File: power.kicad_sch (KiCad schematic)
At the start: 4 parts, among them J1 USB_C_Receptacle_USB2.0_16P, U2 USBLC6-2SC6

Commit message: add power
Signed-off-by: HaoboGu <haobogu@outlook.com>
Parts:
- added C1, C2: 10uf, symbol Device:C
- added C3, C4: 10uf, symbol Device:C_Polarized_Small_US
- added J2: Battery, Connector_JST:JST_SH_SM02B-SRSS-TB_1x02-1MP_P1.00mm_Horizontal, symbol Connector_Generic_Shielded:Conn_01x02_Shielded
- added R3: 3K, symbol Device:R
- added R4: 0.4, symbol Device:R
- added R5: 10K, symbol Device:R
- added SW62: SW_SPDT, symbol Switch:SW_SPDT
- added U3: TP4056, TP4056:ESOP-8_L4.9-W3.9-P1.27-LS6.0-BL-EP, symbol TP4056:TP4056_C725790
- added U4: AMS1117-3.3, Package_TO_SOT_SMD:SOT-223-3_TabPin2, symbol Regulator_Linear:AMS1117-3.3
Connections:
- net +5V: now also C4.1, R4.1, U4.3 (VI)
- net GND: now also C1.2, C2.2, C3.2, C4.2, J2.2 (Pin_2), J2.SH (Shield), R3.1, U3.1 (TEMP), U3.3 (GND), U4.1 (GND)
- new net: J2.1 (Pin_1), SW62.2 (B)
- new net: R5.2, SW62.3 (C)
- new net: R3.2, U3.2 (PROG)
- new net +3.3V: C3.1, U4.2 (VO)
- new net CHARGE: U3.7 (CHRG#)
- new net Li+: C1.1, SW62.1 (A), U3.5 (BAT)
- new net Vin: C2.1, R4.2, U3.4 (VCC), U3.8 (CE)
- no-connect marks 2 -> 5
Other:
- note added: "5V -> 3.3V"
- note added: "Battery"
- note added: "ESD"
- note added: "I_bat = 400ma"
- note added: "USB"
- moved on the sheet: J1, R1, R2, U2

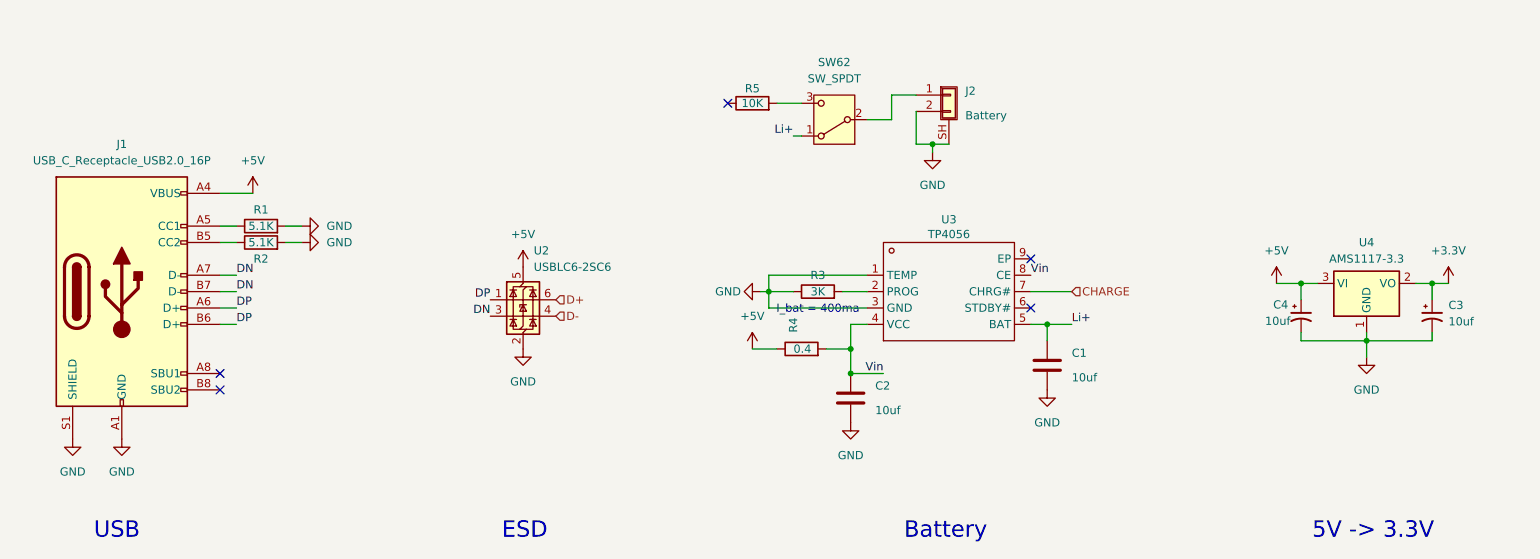
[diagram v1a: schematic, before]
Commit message: schema: rev0 done
Signed-off-by: HaoboGu <haobogu@outlook.com>
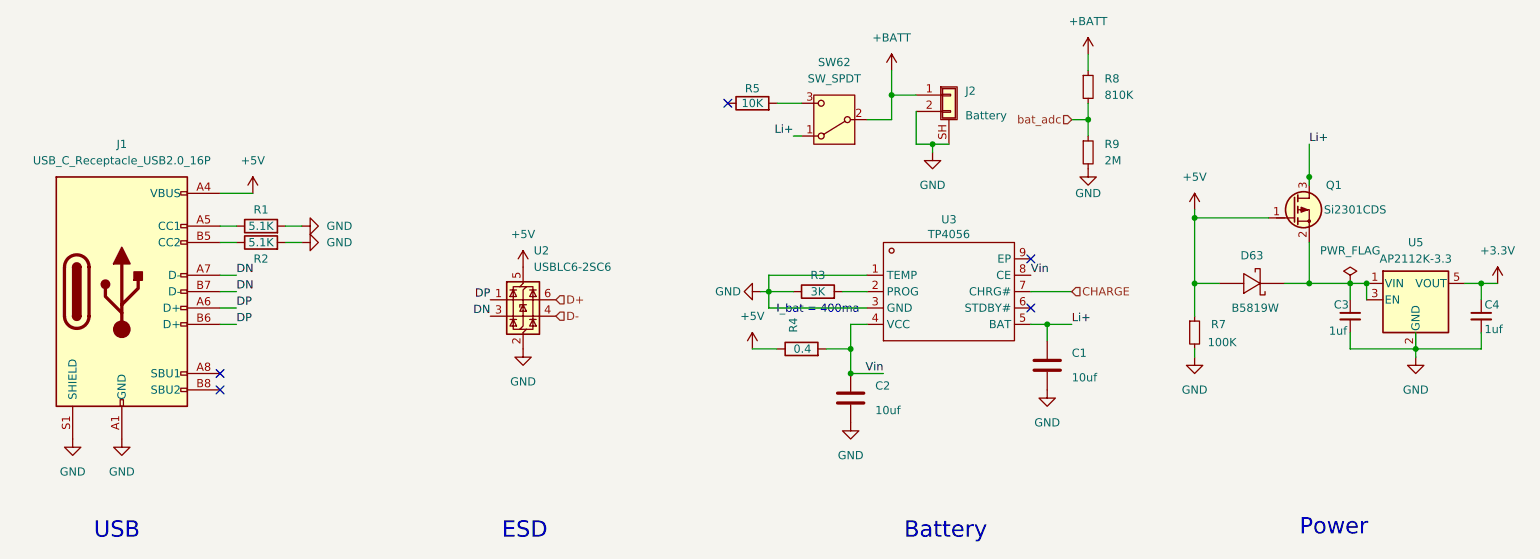
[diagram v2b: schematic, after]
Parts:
- removed C3, C4: 10uf, symbol Device:C_Polarized_Small_US
- removed U4: AMS1117-3.3, Package_TO_SOT_SMD:SOT-223-3_TabPin2, symbol Regulator_Linear:AMS1117-3.3
- added C3, C4: 1uf, symbol Device:C_Small
- added D63: B5819W, B5819W-SL:SOD-123_L2.7-W1.6-LS3.7-RD-1, symbol B5819W-SL:B5819W_C8598
- added Q1: Si2301CDS, Package_TO_SOT_SMD_AKL:SOT-23, symbol PCM_Transistor_MOSFET_AKL:Si2301CDS
- added R7: 100K, symbol Device:R_Small
- added R8: 810K, jiran-ble-lite:R_0603, symbol Device:R_Small
- added R9: 2M, jiran-ble-lite:R_0603, symbol Device:R_Small
- added U5: AP2112K-3.3, Package_TO_SOT_SMD:SOT-23-5, symbol Regulator_Linear:AP2112K-3.3
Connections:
- net +3.3V: now also C4.1, U5.5 (VOUT)
- net +5V: now also D63.2 (+), Q1.1 (G), R7.1
- net GND: now also C3.2, C4.2, R7.2, R9.2, U5.2 (GND)
- net Li+: now also Q1.3 (D)
- net +BATT: now reaches J2.1 (Pin_1), SW62.2 (B)
- net +BATT: now also R8.1
- new net: C3.1, D63.1 (-), Q1.2 (S), U5.1 (VIN), U5.3 (EN)
- new net bat_adc: R8.2, R9.1
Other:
- note added: "Power"
- note removed: "5V -> 3.3V"

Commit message: assign footprints
Signed-off-by: HaoboGu <haobogu@outlook.com>
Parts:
- C1, C2, C3, C4: footprint (none) -> Capacitor_SMD:C_0603_1608Metric_Pad1.08x0.95mm_HandSolder
- J1: footprint (none) -> Connector_USB:USB_C_Receptacle_GCT_USB4105-xx-A_16P_TopMnt_Horizontal
- Q1: footprint Package_TO_SOT_SMD_AKL:SOT-23 -> Package_TO_SOT_SMD:SOT-23-5_HandSoldering
- R1, R2, R3, R5, R7: footprint (none) -> Resistor_SMD:R_0603_1608Metric_Pad0.98x0.95mm_HandSolder
- R4: footprint (none) -> Resistor_SMD:R_0805_2012Metric_Pad1.20x1.40mm_HandSolder
- R8, R9: footprint jiran-ble-lite:R_0603 -> Resistor_SMD:R_0603_1608Metric_Pad0.98x0.95mm_HandSolder
- SW62: value SW_SPDT -> MSK-12C02; footprint (none) -> MSK-12C02:SW-TH_MSK12C02
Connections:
- net +3.3V renamed 3V3
- net +5V renamed VBUS
- net +BATT: no longer names the net of J2.1 (Pin_1), R8.1, SW62.2 (B)
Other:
- moved on the sheet: R8, R9

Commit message: pcb layout
Signed-off-by: HaoboGu <haobogu@outlook.com>
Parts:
- removed J2: Battery, Connector_JST:JST_SH_SM02B-SRSS-TB_1x02-1MP_P1.00mm_Horizontal, symbol Connector_Generic_Shielded:Conn_01x02_Shielded
- added J6: Battery, Connector_JST:JST_SH_SM02B-SRSS-TB_1x02-1MP_P1.00mm_Horizontal, symbol Connector_Generic_MountingPin:Conn_02x01_MountingPin
- Q1: footprint Package_TO_SOT_SMD:SOT-23-5_HandSoldering -> Package_TO_SOT_SMD:SOT-23
- SW62: footprint MSK-12C02:SW-TH_MSK12C02 -> Button_Switch_SMD:SW_SPDT_PCM12
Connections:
- net GND: now also J6.2 (Pin_2), J6.MP (MountPin)
- net at R8.1, SW62.2 (B): now also J6.1 (Pin_1)
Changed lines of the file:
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@@
 	)
 	(junction
+		(at 186.69 41.91)
+		(diameter 0)
+		(color 0 0 0 0)
+	)
+	(junction
 		(at 257.81 76.2)
 		(diameter 0)
@@
 		(color 0 0 0 0)
 	)
-	(junction
-		(at 182.88 44.45)
-		(diameter 0)
-		(color 0 0 0 0)
-	)
 	(no_connect
 		(at 198.12 69.85)
@@
 	(wire
 		(pts
-			(xy 182.88 44.45) (xy 185.42 44.45)
-		)
-		(stroke
-			(width 0)
-			(type default)
-		)
-	)
-	(wire
-		(pts
 			(xy 157.48 69.85) (xy 172.72 69.85)
 		)
@@
 	(wire
 		(pts
-			(xy 180.34 39.37) (xy 180.34 44.45)
+			(xy 223.52 55.88) (xy 223.52 66.04)
 		)
 		(stroke
@@
 	(wire
 		(pts
-			(xy 223.52 55.88) (xy 223.52 66.04)
+			(xy 190.5 41.91) (xy 186.69 41.91)
 		)
 		(stroke
@@
 	(wire
 		(pts
-			(xy 180.34 44.45) (xy 182.88 44.45)
-		)
-		(stroke
-			(width 0)
-			(type default)
-		)
-	)
-	(wire
-		(pts
-			(xy 182.88 45.72) (xy 182.88 44.45)
-		)
-		(stroke
-			(width 0)
-			(type default)
-		)
-	)
-	(wire
-		(pts
 			(xy 175.26 80.01) (xy 170.18 80.01)
 		)
@@
 	(wire
 		(pts
-			(xy 176.53 36.83) (xy 180.34 36.83)
+			(xy 176.53 36.83) (xy 177.8 36.83)
 		)
 		(stroke
@@
 	(wire
 		(pts
+			(xy 184.15 41.91) (xy 186.69 41.91)
+		)
+		(stroke
+			(width 0)
+			(type default)
+		)
+	)
+	(wire
+		(pts
 			(xy 267.97 66.04) (xy 267.97 68.58)
 		)
@@
 	(wire
 		(pts
+			(xy 190.5 36.83) (xy 190.5 41.91)
+		)
+		(stroke
+			(width 0)
+			(type default)
+		)
+	)
+	(wire
+		(pts
 			(xy 196.85 29.21) (xy 196.85 31.75)
 		)
@@
 			)
 		)
-		(property "Footprint" "MSK-12C02:SW-TH_MSK12C02"
+		(property "Footprint" "Button_Switch_SMD:SW_SPDT_PCM12"
 			(at 167.64 40.64 0)
 			(effects
@@
 	)
 	(symbol
-		(lib_id "Connector_Generic_Shielded:Conn_01x02_Shielded")
-		(at 185.42 36.83 0)
-		(unit 1)
-		(exclude_from_sim no)
-		(in_bom yes)
-		(on_board yes)
-		(dnp no)
-		(property "Reference" "J2"
-			(at 187.96 36.1949 0)
-			(effects
-				(font
-					(size 1.27 1.27)
-				)
-				(justify left)
-			)
-		)
-		(property "Value" "Battery"
-			(at 187.96 40.0049 0)
-			(effects
-				(font
-					(size 1.27 1.27)
-				)
-				(justify left)
-			)
-		)
-		(property "Footprint" "Connector_JST:JST_SH_SM02B-SRSS-TB_1x02-1MP_P1.00mm_Horizontal"
-			(at 185.42 36.83 0)
-			(effects
-				(font
-					(size 1.27 1.27)
-				)
-				(hide yes)
-			)
-		)
-		(property "Datasheet" "~"
-			(at 185.42 36.83 0)
-			(effects
-				(font
-					(size 1.27 1.27)
-				)
-				(hide yes)
-			)
-		)
-		(property "Description" "Generic shielded connector, single row, 01x02, script generated (kicad-library-utils/schlib/autogen/connector/)"
-			(at 185.42 36.83 0)
-			(effects
-				(font
-					(size 1.27 1.27)
-				)
-				(hide yes)
-			)
-		)
-		(pin "SH"
-		)
-		(pin "1"
-		)
-		(pin "2"
-		)
-		(instances
-			(project "rmk-ble-keyboard"
-				(path "/5823a915-d0ed-4262-9b2d-d2247405cf69/80617de3-f245-4e85-9542-0f05c79e7b1e"
-					(reference "J2")
-					(unit 1)
-				)
-			)
-		)
-	)
-	(symbol
 		(lib_id "power:GND")
 		(at 156.21 67.31 270)
@@
 			)
 		)
-		(property "Footprint" "Package_TO_SOT_SMD:SOT-23-5_HandSoldering"
+		(property "Footprint" "Package_TO_SOT_SMD:SOT-23"
 			(at 243.84 52.07 0)
 			(effects
@@
 	(symbol
 		(lib_id "power:GND")
-		(at 182.88 45.72 0)
+		(at 186.69 41.91 0)
 		(unit 1)
 		(exclude_from_sim no)
@@
 		(fields_autoplaced yes)
 		(property "Reference" "#PWR08"
-			(at 182.88 52.07 0)
+			(at 186.69 48.26 0)
 			(effects
 				(font
@@
 		)
 		(property "Value" "GND"
-			(at 182.88 50.8 0)
+			(at 186.69 46.99 0)
 			(effects
 				(font
@@
 		)
 		(property "Footprint" ""
-			(at 182.88 45.72 0)
+			(at 186.69 41.91 0)
 			(effects
 				(font
@@
 		)
 		(property "Datasheet" ""
-			(at 182.88 45.72 0)
+			(at 186.69 41.91 0)
 			(effects
 				(font
@@
 		)
 		(property "Description" "Power symbol creates a global label with name \"GND\" , ground"
-			(at 182.88 45.72 0)
+			(at 186.69 41.91 0)
 			(effects
 				(font
@@
 					(unit 1)
 				)
+			)
+		)
+	)
+	(symbol
+		(lib_id "Connector_Generic_MountingPin:Conn_02x01_MountingPin")
+		(at 182.88 36.83 0)
+		(unit 1)
+		(exclude_from_sim no)
+		(in_bom yes)
+		(on_board yes)
+		(dnp no)
+		(fields_autoplaced yes)
+		(property "Reference" "J6"
+			(at 184.15 30.48 0)
+			(effects
+				(font
+					(size 1.27 1.27)
+				)
+			)
+		)
+		(property "Value" "Battery"
+			(at 184.15 33.02 0)
+			(effects
+				(font
+					(size 1.27 1.27)
+				)
+			)
+		)
+		(property "Footprint" "Connector_JST:JST_SH_SM02B-SRSS-TB_1x02-1MP_P1.00mm_Horizontal"
+			(at 182.88 36.83 0)
+			(effects
+				(font
+					(size 1.27 1.27)
+				)
+				(hide yes)
+			)
+		)
+		(property "Datasheet" "~"
+			(at 182.88 36.83 0)
+			(effects
+				(font
+					(size 1.27 1.27)
+				)
+				(hide yes)
+			)
+		)
+		(property "Description" "Generic connectable mounting pin connector, double row, 02x01, this symbol is compatible with counter-clockwise, top-bottom and odd-even numbering schemes., script generated (kicad-library-utils/schlib/autogen/connector/)"
+			(at 182.88 36.83 0)
+			(effects
+				(font
+					(size 1.27 1.27)
+				)
+				(hide yes)
+			)
+		)
+		(pin "1"
+		)
+		(pin "2"
+		)
+		(pin "MP"
+		)
+		(instances
+			(project "rmk-ble-keyboard"
+				(path "/5823a915-d0ed-4262-9b2d-d2247405cf69/80617de3-f245-4e85-9542-0f05c79e7b1e"
+					(reference "J6")
+					(unit 1)
+				)

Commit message: rev 1.0
Signed-off-by: HaoboGu <haobogu@outlook.com>
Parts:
- J6: value Battery -> JST-SM02B-SRSS-TB
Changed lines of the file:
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@@
 			)
 		)
-		(property "Value" "Battery"
+		(property "Value" "JST-SM02B-SRSS-TB"
 			(at 184.15 33.02 0)
 			(effects

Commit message: update production file
Signed-off-by: HaoboGu <haobogu@outlook.com>
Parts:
- R8: value 810K -> 820K
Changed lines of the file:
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@@
 			)
 		)
-		(property "Value" "810K"
+		(property "Value" "820K"
 			(at 199.39 35.5599 0)
 			(effects

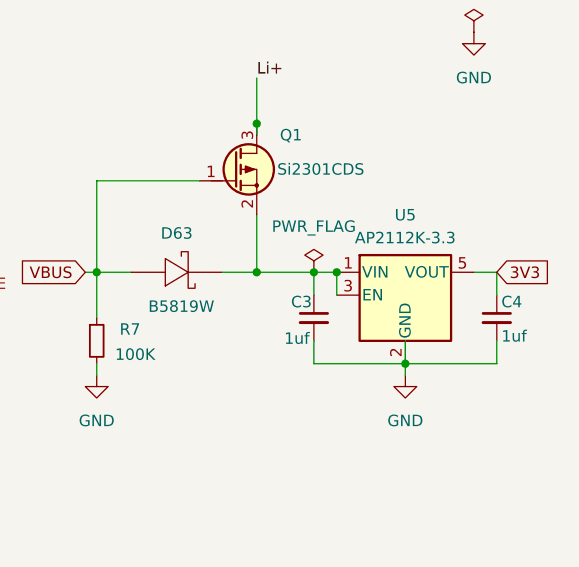
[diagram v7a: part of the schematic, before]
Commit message: feat: use xc6202 to replace ap2112k
Signed-off-by: HaoboGu <haobogu@outlook.com>
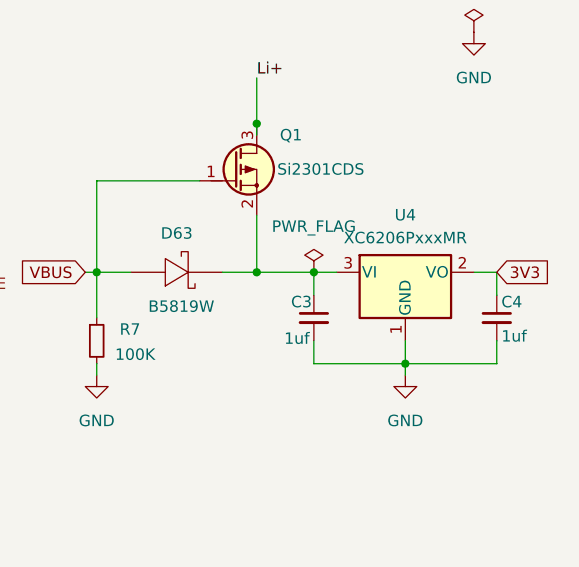
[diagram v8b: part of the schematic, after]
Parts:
- removed U5: AP2112K-3.3, Package_TO_SOT_SMD:SOT-23-5, symbol Regulator_Linear:AP2112K-3.3
- added U4: XC6206PxxxMR, Package_TO_SOT_SMD:SOT-23-3, symbol Regulator_Linear:XC6206PxxxMR
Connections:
- net 3V3: now also U4.2 (VO)
- net GND: now also U4.1 (GND)
- net at C3.1, D63.1 (-), Q1.2 (S): now also U4.3 (VI)
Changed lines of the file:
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@@
 	)
 	(junction
-		(at 250.19 66.04)
-		(diameter 0)
-		(color 0 0 0 0)
-	)
-	(junction
 		(at 223.52 66.04)
 		(diameter 0)
@@
 	(wire
 		(pts
-			(xy 250.19 66.04) (xy 250.19 68.58)
-		)
-		(stroke
-			(width 0)
-			(type default)
-		)
-	)
-	(wire
-		(pts
 			(xy 247.65 76.2) (xy 247.65 73.66)
 		)
@@
 	(wire
 		(pts
+			(xy 267.97 66.04) (xy 267.97 68.58)
+		)
+		(stroke
+			(width 0)
+			(type default)
+		)
+	)
+	(wire
+		(pts
 			(xy 237.49 66.04) (xy 241.3 66.04)
 		)
@@
 	(wire
 		(pts
-			(xy 267.97 66.04) (xy 267.97 68.58)
-		)
-		(stroke
-			(width 0)
-			(type default)
-		)
-	)
-	(wire
-		(pts
 			(xy 168.91 67.31) (xy 172.72 67.31)
 		)
@@
 		(length 2.54)
 		(shape round)
-		(at 267.97 66.04 0)
+		(at 267.97 67.31 0)
 		(fields_autoplaced yes)
 		(effects
@@
 		)
 		(property "Netclass" "Power"
-			(at 268.6685 63.5 0)
+			(at 268.6685 64.77 0)
 			(effects
 				(font
@@
 	)
 	(symbol
-		(lib_id "Regulator_Linear:AP2112K-3.3")
-		(at 257.81 68.58 0)
-		(unit 1)
-		(exclude_from_sim no)
-		(in_bom yes)
-		(on_board yes)
-		(dnp no)
-		(fields_autoplaced yes)
-		(property "Reference" "U5"
-			(at 257.81 59.69 0)
-			(effects
-				(font
-					(size 1.27 1.27)
-				)
-			)
-		)
-		(property "Value" "AP2112K-3.3"
-			(at 257.81 62.23 0)
-			(effects
-				(font
-					(size 1.27 1.27)
-				)
-			)
-		)
-		(property "Footprint" "Package_TO_SOT_SMD:SOT-23-5"
-			(at 257.81 60.325 0)
-			(effects
-				(font
-					(size 1.27 1.27)
-				)
-				(hide yes)
-			)
-		)
-		(property "Datasheet" "https://www.diodes.com/assets/Datasheets/AP2112.pdf"
-			(at 257.81 66.04 0)
-			(effects
-				(font
-					(size 1.27 1.27)
-				)
-				(hide yes)
-			)
-		)
-		(property "Description" "600mA low dropout linear regulator, with enable pin, 3.8V-6V input voltage range, 3.3V fixed positive output, SOT-23-5"
-			(at 257.81 68.58 0)
-			(effects
-				(font
-					(size 1.27 1.27)
-				)
-				(hide yes)
-			)
-		)
-		(pin "1"
-		)
-		(pin "3"
-		)
-		(pin "5"
-		)
-		(pin "4"
-		)
-		(pin "2"
-		)
-		(instances
-			(project "rmk-ble-keyboard"
-				(path "/5823a915-d0ed-4262-9b2d-d2247405cf69/80617de3-f245-4e85-9542-0f05c79e7b1e"
-					(reference "U5")
-					(unit 1)
-				)
-			)
-		)
-	)
-	(symbol
 		(lib_id "Device:C_Small")
 		(at 247.65 71.12 0)
@@
 					(unit 1)
 				)
+			)
+		)
+	)
+	(symbol
+		(lib_id "Regulator_Linear:XC6206PxxxMR")
+		(at 257.81 66.04 0)
+		(unit 1)
+		(exclude_from_sim no)
+		(in_bom yes)
+		(on_board yes)
+		(dnp no)
+		(fields_autoplaced yes)
+		(property "Reference" "U4"
+			(at 257.81 59.69 0)
+			(effects
+				(font
+					(size 1.27 1.27)
+				)
+			)
+		)
+		(property "Value" "XC6206PxxxMR"
+			(at 257.81 62.23 0)
+			(effects
+				(font
+					(size 1.27 1.27)
+				)
+			)
+		)
+		(property "Footprint" "Package_TO_SOT_SMD:SOT-23-3"
+			(at 257.81 60.325 0)
+			(effects
+				(font
+					(size 1.27 1.27)
+					(italic yes)
+				)
+				(hide yes)
+			)
+		)
+		(property "Datasheet" "https://www.torexsemi.com/file/xc6206/XC6206.pdf"
+			(at 257.81 66.04 0)
+			(effects
+				(font
+					(size 1.27 1.27)
+				)
+				(hide yes)
+			)
+		)
+		(property "Description" "Positive 60-250mA Low Dropout Regulator, Fixed Output, SOT-23"
+			(at 257.81 66.04 0)
+			(effects
+				(font
+					(size 1.27 1.27)
+				)
+				(hide yes)
+			)
+		)
+		(pin "2"
+		)
+		(pin "3"
+		)
+		(pin "1"
+		)
+		(instances
+			(project ""
+				(path "/5823a915-d0ed-4262-9b2d-d2247405cf69/80617de3-f245-4e85-9542-0f05c79e7b1e"
+					(reference "U4")
+					(unit 1)
+				)
